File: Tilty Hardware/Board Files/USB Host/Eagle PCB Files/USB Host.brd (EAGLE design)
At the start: 38.1 x 50.8 mm, 14 parts, among them Q1 12MHz, U1 MAX3421E

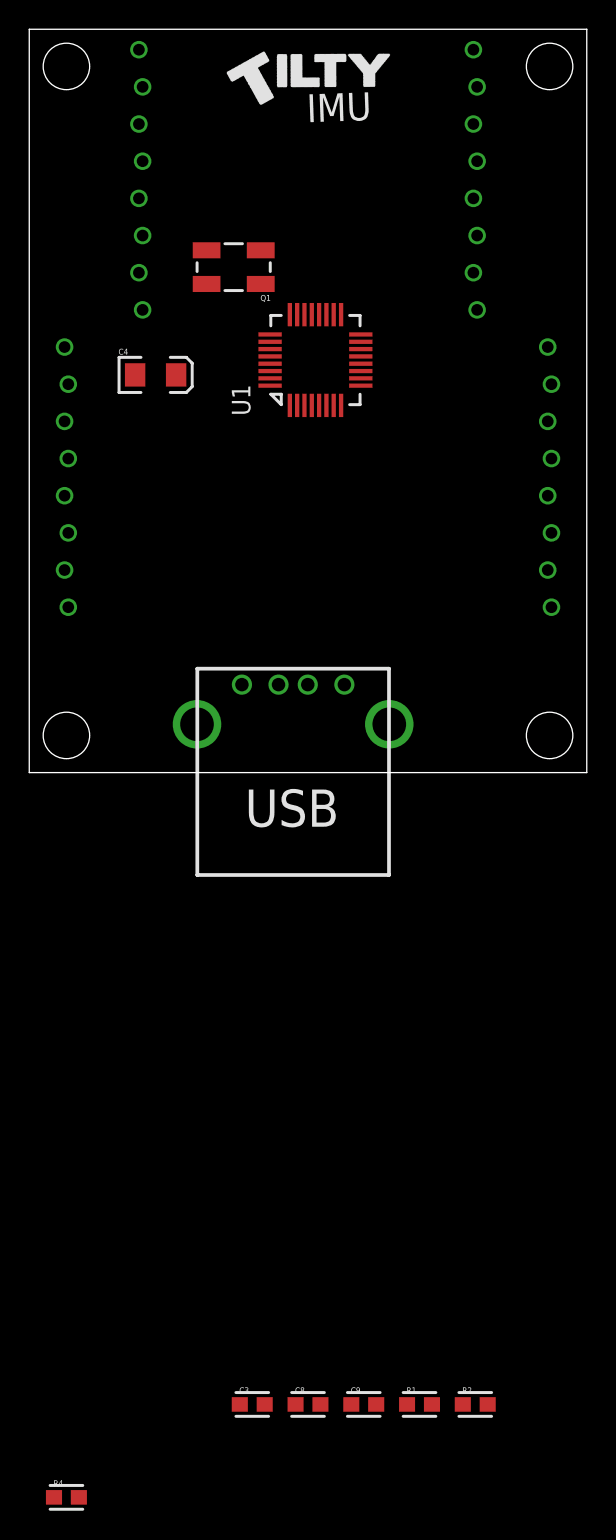
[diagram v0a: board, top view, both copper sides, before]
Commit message: Added some datasheets, USB Host work
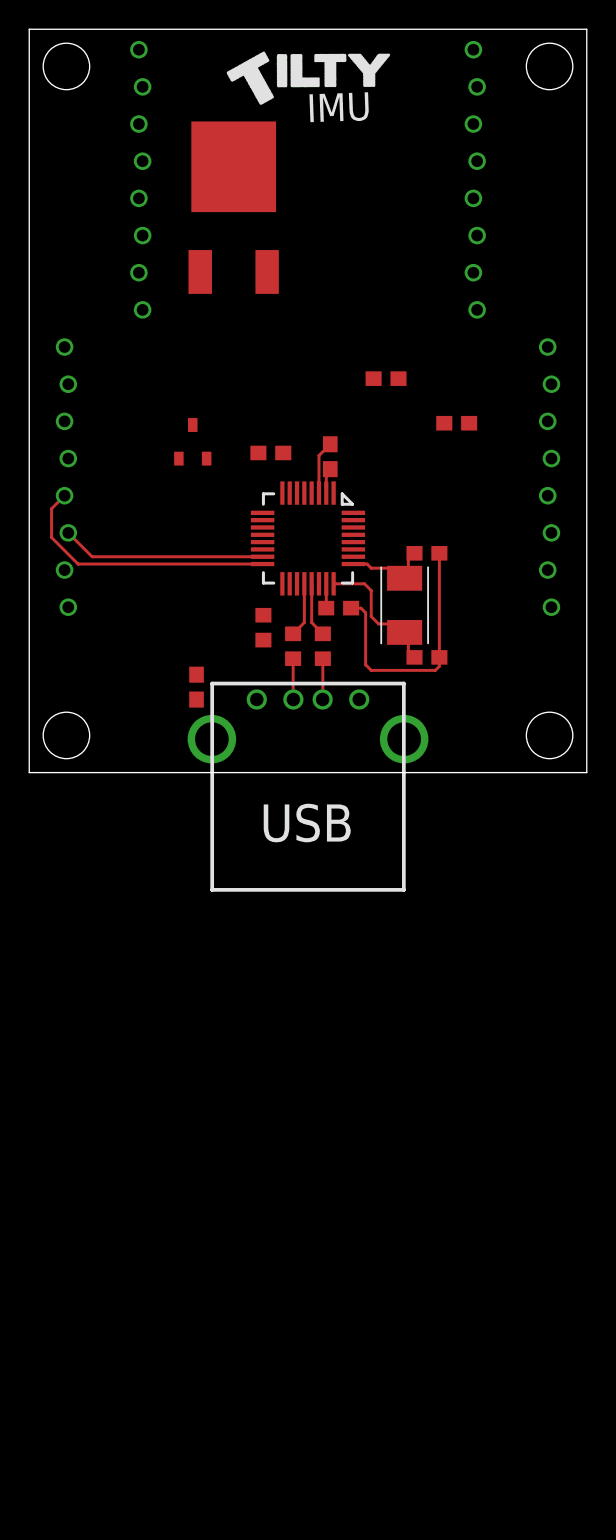
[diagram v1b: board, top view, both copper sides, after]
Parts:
- removed C9: 18pF, CH_passive:0603
- removed Q1: 12MHz, CH_passive:CRYSTAL-SMD-5X3
- removed R4: 2.2K, CH_passive:0603
- added C1, C2, C7: 0.1uF, resistor:C0603
- added C5: 4.7uF, resistor:C0603
- added C6: 1uF, resistor:C0603
- added R3: 4.7K, resistor:R0603
- added U2: AP7313SOT23R, My Parts:SOT23
- added U3: LM2931, on-semiconductor:TO263
- added X1: (no value), SparkFun-FreqCtrl:CRYSTAL-TXC-7A
- C3: value 0.1uF -> 22pF; device CH_passive:0603 -> resistor:C0603
- C4: value 4.7uF -> 22pF; device CH_passive:EIA3216 -> resistor:C0603
- C8: value 18pF -> 4.7uF; device CH_passive:0603 -> resistor:C0603
- R1, R2: value 33 1% -> 33; device CH_passive:0603 -> resistor:R0603
- moved C8 67.8 mm to (29.2, 23.9)
- moved C3 59.4 mm to (27.2, 15.0), turned to 180 degrees
- moved R2 53.3 mm to (18.0, 8.64), turned to 90 degrees
- moved R1 52.2 mm to (20.1, 8.64), turned to 90 degrees
- moved C4 26.8 mm to (27.2, 7.87), turned to 180 degrees
- moved U1 12.2 mm to (19.1, 16.0), turned to 180 degrees
- moved U$1 1.44 mm to (19.1, 2.29)
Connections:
- net MRST renamed RST
- net SS renamed CS
- removed net GPX: U1.17
- removed net N$40: C8.2, Q1.3, U1.25
- removed net N$41: C9.2, Q1.1, U1.24
- removed net SCLK: U1.13
- new net N$11: C4.2, U1.24, X1.P$1
- new net N$12: C3.2, U1.25, X1.P$2
- new net N$15: C6.2, U2.P$1
- new net N$16: C7.2, C8.2, U3.P$1
- net +3V3: now also C1.1, C2.1, C6.1, R3.2, U2.P$2; no longer R4.2
- net +5V: now also C5.1, C8.1, U2.P$3, U3.P$3; no longer C3.1, C4.A
- net GND: now also C1.2, C2.2, C3.1, C4.1, C5.2; no longer C3.2, C4.C, C8.1, C9.1, Q1.2, Q1.4
- net INT: now also R3.1; no longer R4.1
- net SCK: now also U1.13
- net VCC: now also C7.1, U3.P$2
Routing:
- net GND: track 0.00 -> 21.4 mm
- net MOSI: track 0.00 -> 18.4 mm
- net MISO: track 0.00 -> 14.0 mm
- net N$11: track 0.00 -> 9.44 mm
- net N$12: track 0.00 -> 5.99 mm
- net N$1: track 0.00 -> 3.73 mm
- net N$2: track 0.00 -> 3.73 mm
- net +3V3: track 0.00 -> 3.42 mm
- net N$3: track 0.00 -> 2.81 mm
- net N$8: track 0.00 -> 2.81 mm

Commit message: Nearly finished USB Host
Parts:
- added D1: (no value), SparkFun-LED:LED-0805
- added JP5, JP6: (no value), SparkFun-Connectors:1X08
- added R4: (no value), resistor:R0603
- moved C8 15.7 mm to (14.5, 29.2), turned to 180 degrees
- moved U2 10.4 mm to (18.0, 30.5)
- moved C7 9.25 mm to (10.9, 29.2)
- moved C5 8.60 mm to (13.3, 14.2), turned to 180 degrees
- moved R3 7.30 mm to (17.0, 17.1), turned to 180 degrees
- moved U$1 7.11 mm to (19.1, 9.40)
- moved C4 6.59 mm to (25.4, 14.2)
- moved C3 6.59 mm to (25.4, 21.3)
- moved C6 6.49 mm to (18.0, 27.9), turned to 180 degrees
- moved X1 6.43 mm to (24.6, 17.8)
- moved R1 6.35 mm to (20.1, 15.0)
- moved R2 6.35 mm to (18.0, 15.0)
- moved C2 5.97 mm to (21.1, 17.2)
- moved U1 5.84 mm to (19.1, 21.8)
- moved C1 5.84 mm to (20.6, 27.4)
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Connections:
- removed net N$15: C6.2, U2.P$1
- removed net N$16: C7.2, C8.2, U3.P$1
- new net N$9: D1.1, R4.2
- net +5V: now also R4.1
- net GI0: now also JP5.1
- net GI1: now also JP5.2
- net GI2: now also JP5.3
- net GI3: now also JP5.4
- net GI4: now also JP5.5
- net GI5: now also JP5.6
- net GI6: now also JP5.7
- net GI7: now also JP5.8
- net GND: now also C6.2, C7.2, C8.2, D1.2, U2.P$1, U3.P$1
- net GO0: now also JP6.1
- net GO1: now also JP6.2
- net GO2: now also JP6.3
- net GO3: now also JP6.4
- net GO4: now also JP6.5
- net GO5: now also JP6.6
- net GO6: now also JP6.7
- net GO7: now also JP6.8
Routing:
- net GND: track 21.4 -> 117.6 mm, vias 0 -> 6
- net +5V: track 0.00 -> 77.5 mm, vias 0 -> 3
- net +3V3: track 3.42 -> 57.2 mm, vias 0 -> 2
- net GI0: track 0.00 -> 27.9 mm, vias 0 -> 1
- net VCC: track 0.00 -> 26.5 mm
- net GI1: track 0.00 -> 25.0 mm, vias 0 -> 1
- net GO7: track 0.00 -> 25.0 mm, vias 0 -> 1
- net GO6: track 0.00 -> 23.5 mm, vias 0 -> 1
- net GO4: track 0.00 -> 21.9 mm, vias 0 -> 1
- net GO5: track 0.00 -> 21.6 mm, vias 0 -> 1
- net SCK: track 0.00 -> 21.2 mm, vias 0 -> 1
- net GI2: track 0.00 -> 21.1 mm, vias 0 -> 1
- net GO2: track 0.00 -> 20.5 mm, vias 0 -> 1
- net GO1: track 0.00 -> 19.6 mm, vias 0 -> 1
- net GO0: track 0.00 -> 19.0 mm
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- added copper zone on layer 16, net GND
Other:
- board text added: "0"
- board text added: "1"
- board text added: "2"
- board text added: "3"
- board text added: "4"
- board text added: "5"
- board text added: "6"
- board text added: "7"
- board text added: "Inputs"
- board text added: "Outputs"
- board text added: "PWR"
- board text added: "USB Host"
- board text added: "v0.1.0"

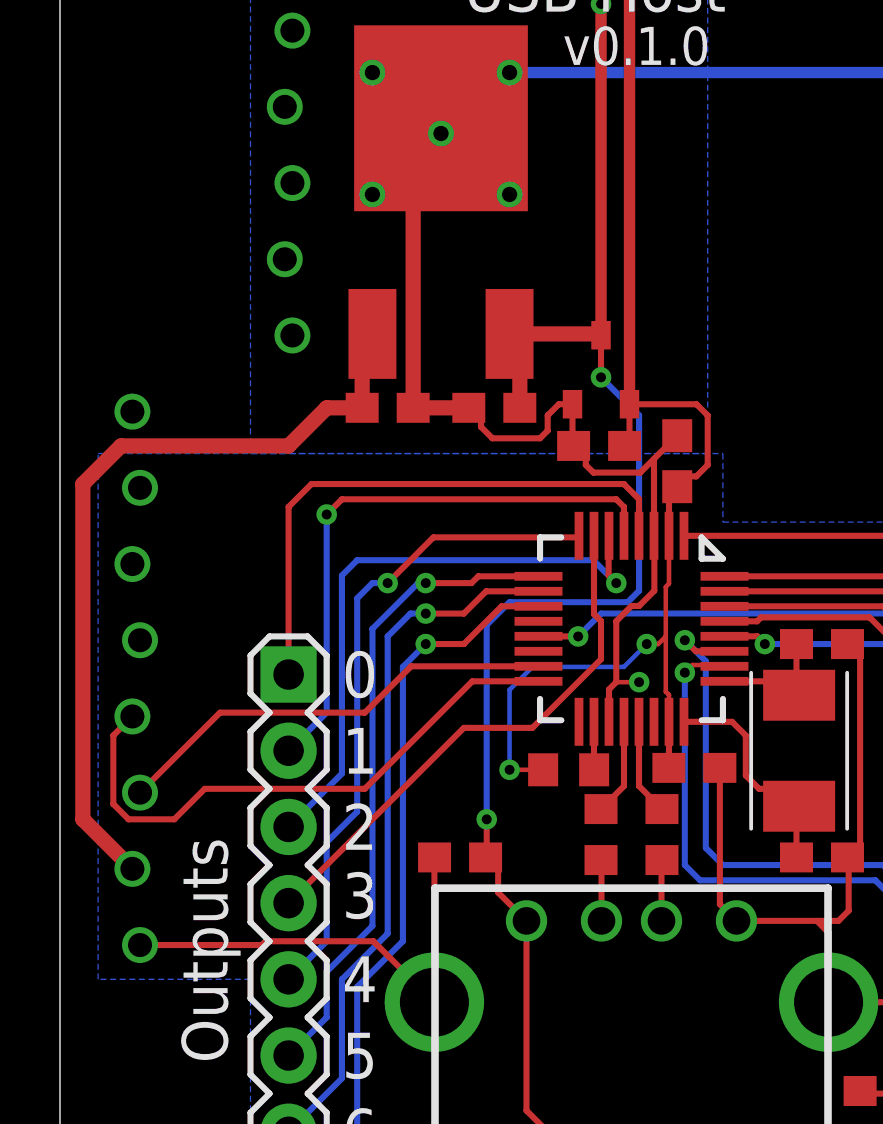
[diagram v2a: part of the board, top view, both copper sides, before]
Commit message: Restarting GPS + Micro SD add-on
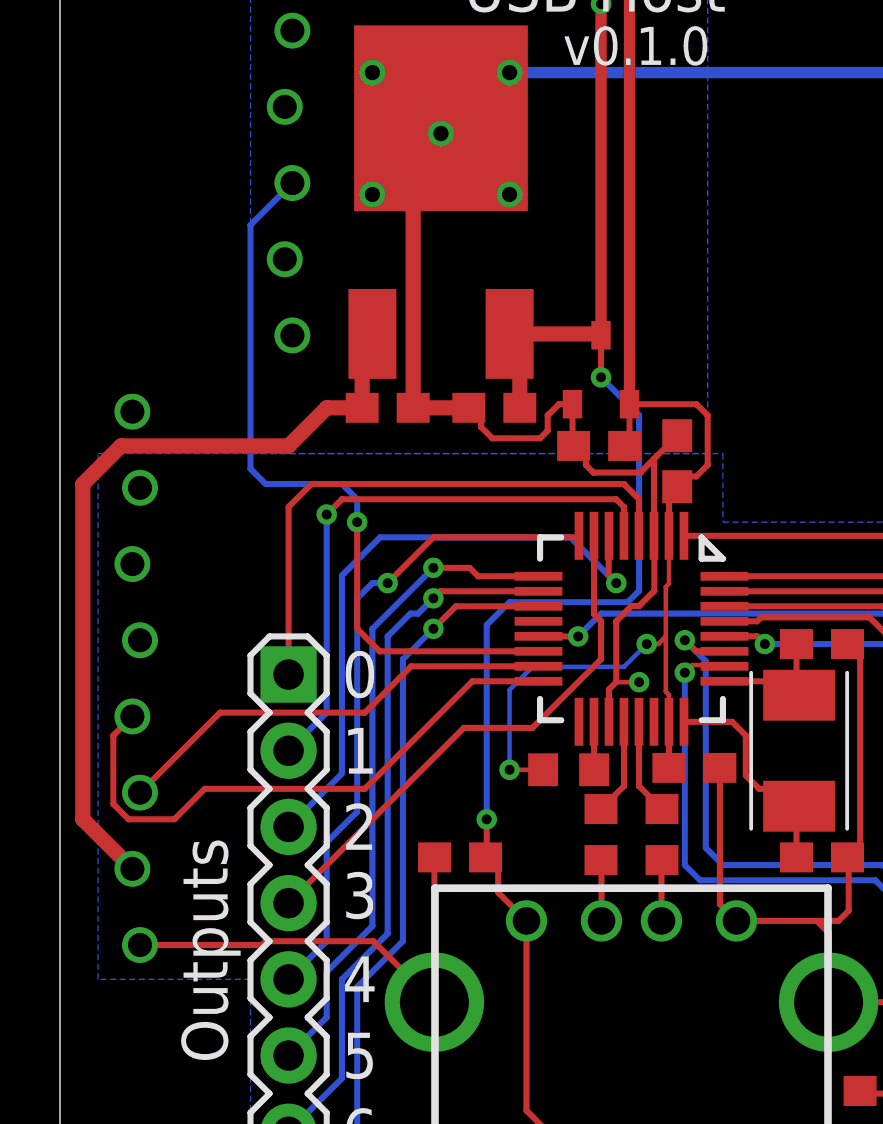
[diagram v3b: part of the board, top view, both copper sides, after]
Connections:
- removed net N$10: JP1.P$6
- net CS: now also JP1.P$6
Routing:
- net CS: track 0.00 -> 24.8 mm, vias 0 -> 1
- net GO2: track 20.5 -> 21.1 mm
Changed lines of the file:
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@@
 <contactref element="JP1" pad="P$7"/>
-</signal>
-<signal name="N$10">
-<contactref element="JP1" pad="P$6"/>
 </signal>
 <signal name="SERVO_2">
@@
 <wire x1="18.288" y1="24.932" x2="18.288" y2="23.622" width="0.2032" layer="1"/>
 <wire x1="18.288" y1="23.622" x2="18.542" y2="23.368" width="0.2032" layer="1"/>
-<wire x1="17.78" y1="24.13" x2="18.542" y2="23.368" width="0.2032" layer="16"/>
-<wire x1="8.89" y1="16.51" x2="8.636" y2="16.256" width="0.2032" layer="16"/>
-<wire x1="8.636" y1="16.256" x2="7.62" y2="15.24" width="0.2032" layer="16"/>
-<wire x1="17.78" y1="24.13" x2="9.906" y2="24.13" width="0.2032" layer="16"/>
-<wire x1="9.906" y1="24.13" x2="9.398" y2="23.622" width="0.2032" layer="16"/>
+<wire x1="9.398" y1="17.018" x2="7.62" y2="15.24" width="0.2032" layer="16"/>
 <wire x1="9.398" y1="23.622" x2="9.398" y2="17.018" width="0.2032" layer="16"/>
-<wire x1="9.398" y1="17.018" x2="8.89" y2="16.51" width="0.2032" layer="16"/>
+<wire x1="18.542" y1="23.368" x2="17.018" y2="24.892" width="0.2032" layer="16"/>
+<wire x1="17.018" y1="24.892" x2="10.668" y2="24.892" width="0.2032" layer="16"/>
+<wire x1="10.668" y1="24.892" x2="9.398" y2="23.622" width="0.2032" layer="16"/>
 </signal>
 <signal name="GO3">
@@
 <contactref element="U1" pad="9"/>
 <contactref element="JP6" pad="6"/>
-<via x="12.192" y="23.368" extent="1-16" drill="0.3302"/>
+<via x="12.446" y="23.876" extent="1-16" drill="0.3302"/>
 <wire x1="15.95" y1="23.594" x2="13.942" y2="23.594" width="0.2032" layer="1"/>
-<wire x1="13.942" y1="23.594" x2="13.716" y2="23.368" width="0.2032" layer="1"/>
-<wire x1="13.716" y1="23.368" x2="12.192" y2="23.368" width="0.2032" layer="1"/>
-<wire x1="12.192" y1="23.368" x2="11.938" y2="23.368" width="0.2032" layer="16"/>
-<wire x1="11.938" y1="23.368" x2="10.414" y2="21.844" width="0.2032" layer="16"/>
+<wire x1="13.942" y1="23.594" x2="13.6525" y2="23.876" width="0.2032" layer="1"/>
+<wire x1="13.6525" y1="23.876" x2="12.446" y2="23.876" width="0.2032" layer="1"/>
+<wire x1="12.446" y1="23.876" x2="10.414" y2="21.844" width="0.2032" layer="16"/>
 <wire x1="10.414" y1="21.844" x2="10.414" y2="11.938" width="0.2032" layer="16"/>
 <wire x1="10.414" y1="11.938" x2="8.89" y2="10.414" width="0.2032" layer="16"/>
@@
 <contactref element="U1" pad="11"/>
 <contactref element="JP6" pad="8"/>
-<via x="12.192" y="21.336" extent="1-16" drill="0.3302"/>
-<wire x1="15.95" y1="22.594" x2="14.72" y2="22.594" width="0.2032" layer="1"/>
-<wire x1="14.72" y1="22.594" x2="13.462" y2="21.336" width="0.2032" layer="1"/>
-<wire x1="13.462" y1="21.336" x2="12.192" y2="21.336" width="0.2032" layer="1"/>
-<wire x1="12.192" y1="21.336" x2="11.43" y2="20.574" width="0.2032" layer="16"/>
-<wire x1="11.43" y1="20.574" x2="11.43" y2="11.43" width="0.2032" layer="16"/>
+<via x="12.446" y="21.844" extent="1-16" drill="0.3302"/>
+<wire x1="11.43" y1="20.828" x2="11.43" y2="11.43" width="0.2032" layer="16"/>
 <wire x1="11.43" y1="11.43" x2="9.906" y2="9.906" width="0.2032" layer="16"/>
 <wire x1="9.906" y1="9.906" x2="9.906" y2="4.826" width="0.2032" layer="16"/>
 <wire x1="9.906" y1="4.826" x2="7.62" y2="2.54" width="0.2032" layer="16"/>
+<wire x1="11.43" y1="20.828" x2="12.446" y2="21.844" width="0.2032" layer="16"/>
+<wire x1="15.95" y1="22.594" x2="13.196" y2="22.594" width="0.2032" layer="1"/>
+<wire x1="13.196" y1="22.594" x2="12.446" y2="21.844" width="0.2032" layer="1"/>
 </signal>
 <signal name="GO6">
 <contactref element="U1" pad="10"/>
 <contactref element="JP6" pad="7"/>
-<via x="12.192" y="22.352" extent="1-16" drill="0.3302"/>
-<wire x1="15.95" y1="23.094" x2="14.204" y2="23.094" width="0.2032" layer="1"/>
-<wire x1="14.204" y1="23.094" x2="13.462" y2="22.352" width="0.2032" layer="1"/>
-<wire x1="13.462" y1="22.352" x2="12.192" y2="22.352" width="0.2032" layer="1"/>
-<wire x1="12.192" y1="22.352" x2="11.684" y2="22.352" width="0.2032" layer="16"/>
-<wire x1="11.684" y1="22.352" x2="10.922" y2="21.59" width="0.2032" layer="16"/>
+<via x="12.446" y="22.86" extent="1-16" drill="0.3302"/>
+<wire x1="15.95" y1="23.094" x2="12.68" y2="23.094" width="0.2032" layer="1"/>
 <wire x1="10.922" y1="21.59" x2="10.922" y2="11.684" width="0.2032" layer="16"/>
 <wire x1="10.922" y1="11.684" x2="9.398" y2="10.16" width="0.2032" layer="16"/>
 <wire x1="9.398" y1="10.16" x2="9.398" y2="6.858" width="0.2032" layer="16"/>
 <wire x1="9.398" y1="6.858" x2="7.62" y2="5.08" width="0.2032" layer="16"/>
+<wire x1="12.446" y1="22.86" x2="11.938" y2="22.352" width="0.2032" layer="16"/>
+<wire x1="11.938" y1="22.352" x2="11.684" y2="22.352" width="0.2032" layer="16"/>
+<wire x1="11.684" y1="22.352" x2="10.922" y2="21.59" width="0.2032" layer="16"/>
+<wire x1="12.68" y1="23.094" x2="12.446" y2="22.86" width="0.2032" layer="1"/>
 </signal>
 <signal name="GI7">
@@
 <signal name="CS">
 <contactref element="U1" pad="14"/>
+<contactref element="JP1" pad="P$6"/>
+<via x="9.906" y="25.4" extent="1-16" drill="0.3302"/>
+<wire x1="15.95" y1="21.094" x2="10.656" y2="21.094" width="0.2032" layer="1"/>
+<wire x1="10.656" y1="21.094" x2="9.906" y2="21.844" width="0.2032" layer="1"/>
+<wire x1="9.906" y1="21.844" x2="9.906" y2="25.4" width="0.2032" layer="1"/>
+<wire x1="9.906" y1="25.4" x2="9.906" y2="26.162" width="0.2032" layer="16"/>
+<wire x1="9.906" y1="26.162" x2="9.398" y2="26.67" width="0.2032" layer="16"/>
+<wire x1="9.398" y1="26.67" x2="6.858" y2="26.67" width="0.2032" layer="16"/>
+<wire x1="6.858" y1="26.67" x2="6.35" y2="27.178" width="0.2032" layer="16"/>
+<wire x1="6.35" y1="27.178" x2="6.35" y2="35.306" width="0.2032" layer="16"/>
+<wire x1="6.35" y1="35.306" x2="7.747" y2="36.703" width="0.2032" layer="16"/>
 </signal>
 <signal name="INT">
